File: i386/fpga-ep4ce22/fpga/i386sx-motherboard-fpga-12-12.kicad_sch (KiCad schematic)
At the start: 1 part, among them U3 (6/6) EP4CE22F17C8N

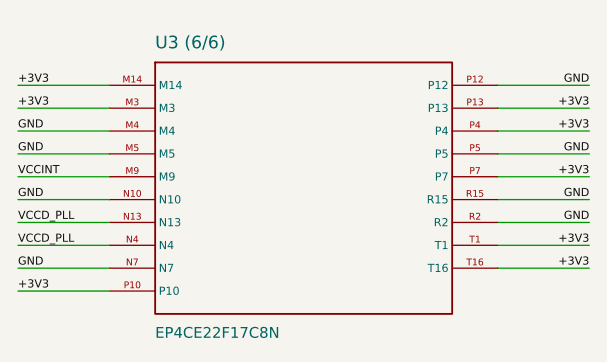
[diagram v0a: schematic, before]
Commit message: Publish the motherboards' KiCad files
From socket3@c0f6464 socket7@9205469 socket370@524f5b1 i386@bea926c
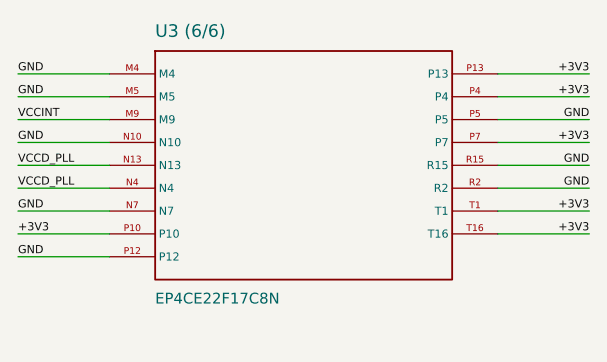
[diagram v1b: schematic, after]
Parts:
- removed U3 (6/6): EP4CE22F17C8N, symbol gen:S10_9
- added U3 (6/6): EP4CE22F17C8N, symbol gen:S9_8
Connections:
- net +3V3: now also U3 (6/6).P10, U3 (6/6).P13, U3 (6/6).P4, U3 (6/6).P7, U3 (6/6).T1, U3 (6/6).T16
- net GND: now also U3 (6/6).M4, U3 (6/6).M5, U3 (6/6).N10, U3 (6/6).N7, U3 (6/6).P12, U3 (6/6).P5, U3 (6/6).R15, U3 (6/6).R2
- net VCCD_PLL: now also U3 (6/6).N13, U3 (6/6).N4
- net VCCINT: now also U3 (6/6).M9
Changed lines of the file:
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@@
     (comment 2 "Local parts are WIRED to their chip; only chip-to-chip and the rails travel by label")
   )
-  (symbol (lib_id "gen:S10_9") (at 60.96 33.02 0) (unit 1) (exclude_from_sim no) (in_bom yes) (on_board yes) (dnp no)
-    (property "Reference" "U3 (6/6)" (at 44.46 17.65 0) (effects (font (size 1.4 1.4)) (justify left bottom)))
-    (property "Value" "EP4CE22F17C8N" (at 44.46 48.39 0) (effects (font (size 1.2 1.2)) (justify left top)))
-    (instances (project "i386sx-motherboard" (path "/0ac398a9-1d89-4090-a36f-db7b4d3d6c0d/afbea8c6-ac9c-4cf5-8977-d4038cdc5efe" (reference "U3") (unit 1))))
+  (symbol (lib_id "gen:S9_8") (at 60.96 30.48 0) (unit 1) (exclude_from_sim no) (in_bom yes) (on_board yes) (dnp no)
+    (property "Reference" "U3 (6/6)" (at 44.46 16.38 0) (effects (font (size 1.4 1.4)) (justify left bottom)))
+    (property "Value" "EP4CE22F17C8N" (at 44.46 44.58 0) (effects (font (size 1.2 1.2)) (justify left top)))
+    (instances (project "i386sx-motherboard" (path "/ea05416d-ce24-4c39-9113-85b33d9a88b0/e075fe52-e431-4b75-91e4-d86867a64b8d" (reference "U3") (unit 1))))
   )
-  (wire (pts (xy 39.38 21.59) (xy 29.22 21.59)) (stroke (width 0) (type default)))
-  (wire (pts (xy 39.38 24.13) (xy 29.22 24.13)) (stroke (width 0) (type default)))
-  (wire (pts (xy 39.38 26.67) (xy 29.22 26.67)) (stroke (width 0) (type default)))
-  (wire (pts (xy 39.38 29.21) (xy 29.22 29.21)) (stroke (width 0) (type default)))
-  (wire (pts (xy 39.38 31.75) (xy 29.22 31.75)) (stroke (width 0) (type default)))
-  (wire (pts (xy 39.38 34.29) (xy 29.22 34.29)) (stroke (width 0) (type default)))
-  (wire (pts (xy 39.38 36.83) (xy 29.22 36.83)) (stroke (width 0) (type default)))
-  (wire (pts (xy 39.38 39.37) (xy 29.22 39.37)) (stroke (width 0) (type default)))
-  (wire (pts (xy 39.38 41.91) (xy 29.22 41.91)) (stroke (width 0) (type default)))
-  (wire (pts (xy 39.38 44.45) (xy 29.22 44.45)) (stroke (width 0) (type default)))
-  (wire (pts (xy 82.54 21.59) (xy 92.70 21.59)) (stroke (width 0) (type default)))
-  (wire (pts (xy 82.54 24.13) (xy 92.70 24.13)) (stroke (width 0) (type default)))
-  (wire (pts (xy 82.54 26.67) (xy 92.70 26.67)) (stroke (width 0) (type default)))
-  (wire (pts (xy 82.54 29.21) (xy 92.70 29.21)) (stroke (width 0) (type default)))
-  (wire (pts (xy 82.54 31.75) (xy 92.70 31.75)) (stroke (width 0) (type default)))
-  (wire (pts (xy 82.54 34.29) (xy 92.70 34.29)) (stroke (width 0) (type default)))
-  (wire (pts (xy 82.54 36.83) (xy 92.70 36.83)) (stroke (width 0) (type default)))
-  (wire (pts (xy 82.54 39.37) (xy 92.70 39.37)) (stroke (width 0) (type default)))
-  (wire (pts (xy 82.54 41.91) (xy 92.70 41.91)) (stroke (width 0) (type default)))
-  (label "+3V3" (at 29.22 21.59 0) (effects (font (size 0.9 0.9)) (justify left bottom)))
-  (label "+3V3" (at 29.22 24.13 0) (effects (font (size 0.9 0.9)) (justify left bottom)))
-  (label "+3V3" (at 29.22 44.45 0) (effects (font (size 0.9 0.9)) (justify left bottom)))
-  (label "+3V3" (at 92.70 24.13 0) (effects (font (size 0.9 0.9)) (justify right bottom)))
-  (label "+3V3" (at 92.70 26.67 0) (effects (font (size 0.9 0.9)) (justify right bottom)))
-  (label "+3V3" (at 92.70 31.75 0) (effects (font (size 0.9 0.9)) (justify right bottom)))
-  (label "+3V3" (at 92.70 39.37 0) (effects (font (size 0.9 0.9)) (justify right bottom)))
-  (label "+3V3" (at 92.70 41.91 0) (effects (font (size 0.9 0.9)) (justify right bottom)))
-  (label "GND" (at 29.22 26.67 0) (effects (font (size 0.9 0.9)) (justify left bottom)))
-  (label "GND" (at 29.22 29.21 0) (effects (font (size 0.9 0.9)) (justify left bottom)))
-  (label "GND" (at 29.22 34.29 0) (effects (font (size 0.9 0.9)) (justify left bottom)))
-  (label "GND" (at 29.22 41.91 0) (effects (font (size 0.9 0.9)) (justify left bottom)))
-  (label "GND" (at 92.70 21.59 0) (effects (font (size 0.9 0.9)) (justify right bottom)))
-  (label "GND" (at 92.70 29.21 0) (effects (font (size 0.9 0.9)) (justify right bottom)))
-  (label "GND" (at 92.70 34.29 0) (effects (font (size 0.9 0.9)) (justify right bottom)))
-  (label "GND" (at 92.70 36.83 0) (effects (font (size 0.9 0.9)) (justify right bottom)))
-  (label "VCCINT" (at 29.22 31.75 0) (effects (font (size 0.9 0.9)) (justify left bottom)))
-  (label "VCCD_PLL" (at 29.22 36.83 0) (effects (font (size 0.9 0.9)) (justify left bottom)))
-  (label "VCCD_PLL" (at 29.22 39.37 0) (effects (font (size 0.9 0.9)) (justify left bottom)))
+  (wire (pts (xy 39.38 20.32) (xy 29.22 20.32)) (stroke (width 0) (type default)))
+  (wire (pts (xy 39.38 22.86) (xy 29.22 22.86)) (stroke (width 0) (type default)))
+  (wire (pts (xy 39.38 25.40) (xy 29.22 25.40)) (stroke (width 0) (type default)))
+  (wire (pts (xy 39.38 27.94) (xy 29.22 27.94)) (stroke (width 0) (type default)))
+  (wire (pts (xy 39.38 30.48) (xy 29.22 30.48)) (stroke (width 0) (type default)))
+  (wire (pts (xy 39.38 33.02) (xy 29.22 33.02)) (stroke (width 0) (type default)))
+  (wire (pts (xy 39.38 35.56) (xy 29.22 35.56)) (stroke (width 0) (type default)))
+  (wire (pts (xy 39.38 38.10) (xy 29.22 38.10)) (stroke (width 0) (type default)))
+  (wire (pts (xy 39.38 40.64) (xy 29.22 40.64)) (stroke (width 0) (type default)))
+  (wire (pts (xy 82.54 20.32) (xy 92.70 20.32)) (stroke (width 0) (type default)))
+  (wire (pts (xy 82.54 22.86) (xy 92.70 22.86)) (stroke (width 0) (type default)))
+  (wire (pts (xy 82.54 25.40) (xy 92.70 25.40)) (stroke (width 0) (type default)))
+  (wire (pts (xy 82.54 27.94) (xy 92.70 27.94)) (stroke (width 0) (type default)))
+  (wire (pts (xy 82.54 30.48) (xy 92.70 30.48)) (stroke (width 0) (type default)))
+  (wire (pts (xy 82.54 33.02) (xy 92.70 33.02)) (stroke (width 0) (type default)))
+  (wire (pts (xy 82.54 35.56) (xy 92.70 35.56)) (stroke (width 0) (type default)))
+  (wire (pts (xy 82.54 38.10) (xy 92.70 38.10)) (stroke (width 0) (type default)))
+  (label "GND" (at 29.22 20.32 0) (effects (font (size 0.9 0.9)) (justify left bottom)))
+  (label "GND" (at 29.22 22.86 0) (effects (font (size 0.9 0.9)) (justify left bottom)))
+  (label "GND" (at 29.22 27.94 0) (effects (font (size 0.9 0.9)) (justify left bottom)))
+  (label "GND" (at 29.22 35.56 0) (effects (font (size 0.9 0.9)) (justify left bottom)))
+  (label "GND" (at 29.22 40.64 0) (effects (font (size 0.9 0.9)) (justify left bottom)))
+  (label "GND" (at 92.70 25.40 0) (effects (font (size 0.9 0.9)) (justify right bottom)))
+  (label "GND" (at 92.70 30.48 0) (effects (font (size 0.9 0.9)) (justify right bottom)))
+  (label "GND" (at 92.70 33.02 0) (effects (font (size 0.9 0.9)) (justify right bottom)))
+  (label "VCCINT" (at 29.22 25.40 0) (effects (font (size 0.9 0.9)) (justify left bottom)))
+  (label "VCCD_PLL" (at 29.22 30.48 0) (effects (font (size 0.9 0.9)) (justify left bottom)))
+  (label "VCCD_PLL" (at 29.22 33.02 0) (effects (font (size 0.9 0.9)) (justify left bottom)))
+  (label "+3V3" (at 29.22 38.10 0) (effects (font (size 0.9 0.9)) (justify left bottom)))
+  (label "+3V3" (at 92.70 20.32 0) (effects (font (size 0.9 0.9)) (justify right bottom)))
+  (label "+3V3" (at 92.70 22.86 0) (effects (font (size 0.9 0.9)) (justify right bottom)))
+  (label "+3V3" (at 92.70 27.94 0) (effects (font (size 0.9 0.9)) (justify right bottom)))
+  (label "+3V3" (at 92.70 35.56 0) (effects (font (size 0.9 0.9)) (justify right bottom)))
+  (label "+3V3" (at 92.70 38.10 0) (effects (font (size 0.9 0.9)) (justify right bottom)))
 )
